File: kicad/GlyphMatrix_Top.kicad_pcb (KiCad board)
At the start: 2 copper layers, 294.9 x 128.6 mm, 74 parts

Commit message: added MCU
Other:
- board size 294.9 x 128.6 mm -> 295 x 128.6 mm

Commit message: screw holes
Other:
- board size 295 x 128.6 mm -> 294.9 x 128.6 mm

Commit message: pogo pin - ergogen
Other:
- board size 294.9 x 128.6 mm -> 295 x 128.6 mm

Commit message: changed screw sizes
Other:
- board size 295 x 128.6 mm -> 298.4 x 128.6 mm
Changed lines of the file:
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@@
   (title_block
     (title "GlyphMatrix_Top")
-    (date "2025-07-04")
-    (rev "0.3.6")
+    (date "2025-07-08")
+    (rev "0.4.3")
     (company "Allen Choi")
   )
@@
         (fp_rect (start -59.53125 -9.525) (end 59.53125 9.525) (stroke (width 0.1) (type solid)) (fill no) (layer "Dwgs.User") )
             )
-  (gr_line (start 60.875 202.3) (end 60.875 77.7125) (layer Edge.Cuts) (stroke (width 0.15) (type default)))
-(gr_line (start 62.875 75.7125) (end 353.82500000000005 75.7125) (layer Edge.Cuts) (stroke (width 0.15) (type default)))
-(gr_line (start 355.82500000000005 77.7125) (end 355.82500000000005 202.3) (layer Edge.Cuts) (stroke (width 0.15) (type default)))
-(gr_line (start 353.82500000000005 204.3) (end 62.875 204.3) (layer Edge.Cuts) (stroke (width 0.15) (type default)))
-(gr_arc (start 62.875 75.7125) (mid 61.4607864 76.29828640000001) (end 60.875 77.7125) (layer Edge.Cuts) (stroke (width 0.15) (type default)))
-(gr_arc (start 355.82500000000005 77.7125) (mid 355.2392136 76.29828640000001) (end 353.82500000000005 75.7125) (layer Edge.Cuts) (stroke (width 0.15) (type default)))
-(gr_arc (start 353.82500000000005 204.3) (mid 355.2392136 203.71421360000002) (end 355.82500000000005 202.3) (layer Edge.Cuts) (stroke (width 0.15) (type default)))
-(gr_arc (start 60.875 202.3) (mid 61.4607864 203.71421360000002) (end 62.875 204.3) (layer Edge.Cuts) (stroke (width 0.15) (type default)))
-(gr_circle (center 64.875 79.7125) (end 66.725 79.7125) (layer Edge.Cuts) (stroke (width 0.15) (type default)) (fill none))
-(gr_circle (center 351.82500000000005 79.7125) (end 353.67500000000007 79.7125) (layer Edge.Cuts) (stroke (width 0.15) (type default)) (fill none))
-(gr_circle (center 351.82500000000005 200.3) (end 353.67500000000007 200.3) (layer Edge.Cuts) (stroke (width 0.15) (type default)) (fill none))
-(gr_circle (center 64.875 200.3) (end 66.725 200.3) (layer Edge.Cuts) (stroke (width 0.15) (type default)) (fill none))
-(gr_circle (center 207.75 79.7125) (end 209.6 79.7125) (layer Edge.Cuts) (stroke (width 0.15) (type default)) (fill none))
-(gr_circle (center 214.73125000000002 190.0125) (end 216.58125 190.0125) (layer Edge.Cuts) (stroke (width 0.15) (type default)) (fill none))
-(gr_circle (center 151.21249999999998 141.625) (end 153.06249999999997 141.625) (layer Edge.Cuts) (stroke (width 0.15) (type default)) (fill none))
-(gr_circle (center 265.51250000000005 141.625) (end 267.36250000000007 141.625) (layer Edge.Cuts) (stroke (width 0.15) (type default)) (fill none))
+  (gr_line (start 59.175 202.3) (end 59.175 77.7125) (layer Edge.Cuts) (stroke (width 0.15) (type default)))
+(gr_line (start 61.175 75.7125) (end 355.52500000000003 75.7125) (layer Edge.Cuts) (stroke (width 0.15) (type default)))
+(gr_line (start 357.52500000000003 77.7125) (end 357.52500000000003 202.3) (layer Edge.Cuts) (stroke (width 0.15) (type default)))
+(gr_line (start 355.52500000000003 204.3) (end 61.175 204.3) (layer Edge.Cuts) (stroke (width 0.15) (type default)))
+(gr_arc (start 61.175 75.7125) (mid 59.7607864 76.29828640000001) (end 59.175 77.7125) (layer Edge.Cuts) (stroke (width 0.15) (type default)))
+(gr_arc (start 357.52500000000003 77.7125) (mid 356.9392136 76.29828640000001) (end 355.52500000000003 75.7125) (layer Edge.Cuts) (stroke (width 0.15) (type default)))
+(gr_arc (start 355.52500000000003 204.3) (mid 356.9392136 203.71421360000002) (end 357.52500000000003 202.3) (layer Edge.Cuts) (stroke (width 0.15) (type default)))
+(gr_arc (start 59.175 202.3) (mid 59.7607864 203.71421360000002) (end 61.175 204.3) (layer Edge.Cuts) (stroke (width 0.15) (type default)))
+(gr_circle (center 64.875 79.7125) (end 66.125 79.7125) (layer Edge.Cuts) (stroke (width 0.15) (type default)) (fill none))
+(gr_circle (center 351.82500000000005 79.7125) (end 353.07500000000005 79.7125) (layer Edge.Cuts) (stroke (width 0.15) (type default)) (fill none))
+(gr_circle (center 351.82500000000005 200.3) (end 353.07500000000005 200.3) (layer Edge.Cuts) (stroke (width 0.15) (type default)) (fill none))
+(gr_circle (center 64.875 200.3) (end 66.125 200.3) (layer Edge.Cuts) (stroke (width 0.15) (type default)) (fill none))
+(gr_circle (center 207.75 79.7125) (end 209 79.7125) (layer Edge.Cuts) (stroke (width 0.15) (type default)) (fill none))
+(gr_circle (center 214.73125000000002 190.0125) (end 215.98125000000002 190.0125) (layer Edge.Cuts) (stroke (width 0.15) (type default)) (fill none))
+(gr_circle (center 151.21249999999998 141.625) (end 152.46249999999998 141.625) (layer Edge.Cuts) (stroke (width 0.15) (type default)) (fill none))
+(gr_circle (center 265.51250000000005 141.625) (end 266.76250000000005 141.625) (layer Edge.Cuts) (stroke (width 0.15) (type default)) (fill none))
 )

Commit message: fixed positions for screw holes
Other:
- board size 298.4 x 128.6 mm -> 298.3 x 128.6 mm

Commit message: more tweaks  (#3)
* small tweaks

* GlyphMatrix - 3mm screws

* PhaseShift - 3mm screws

* DeltaForm - 3mm screws

* updated README.md
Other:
- outline, holes or cut-outs redrawn

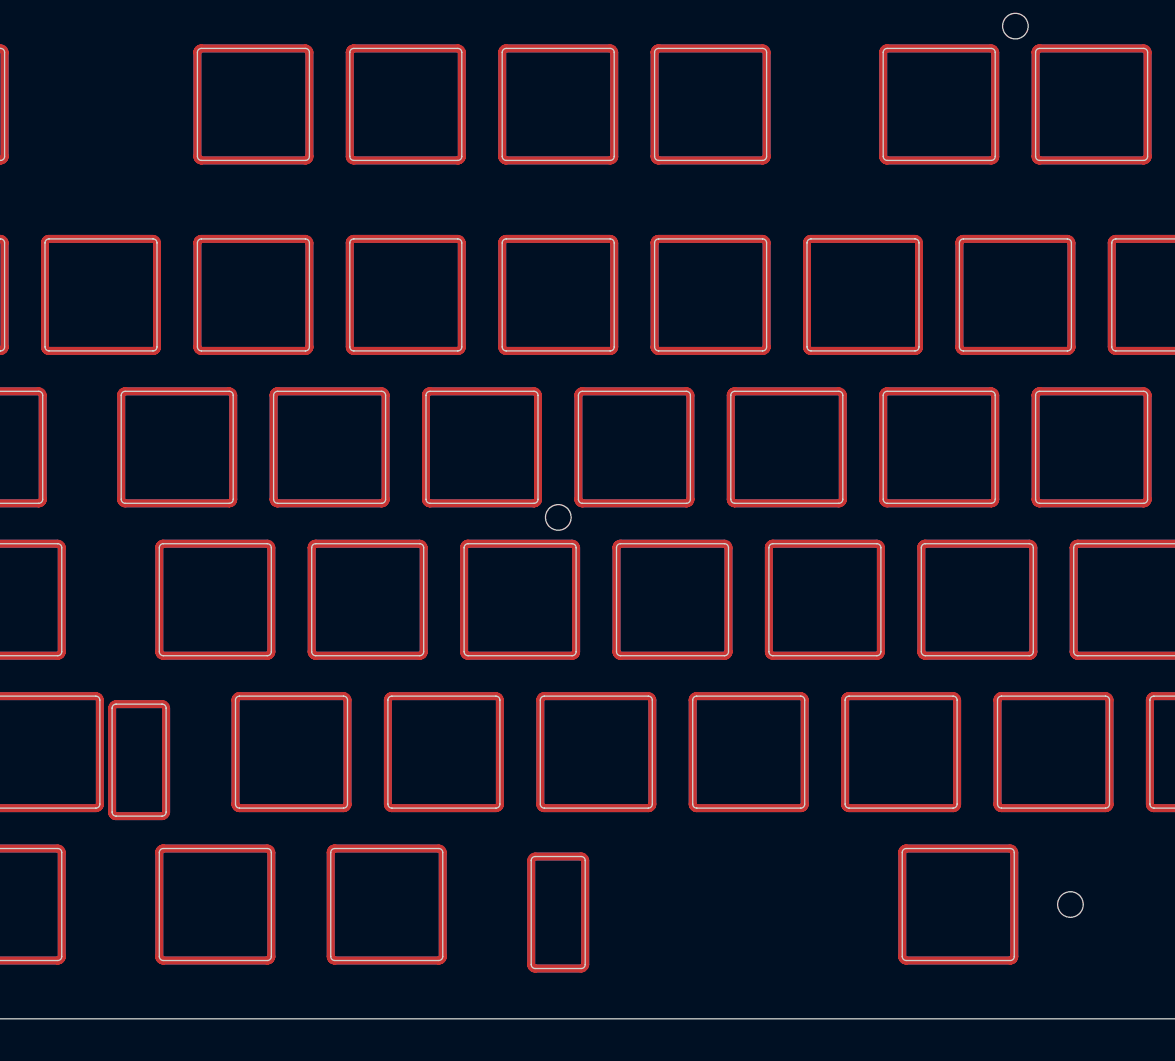
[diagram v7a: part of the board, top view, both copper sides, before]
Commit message: plates (#4)
* Silk Screen

* small changes for GlyphMatrix

* Silk screen for plates

* amended GlyphMatrix
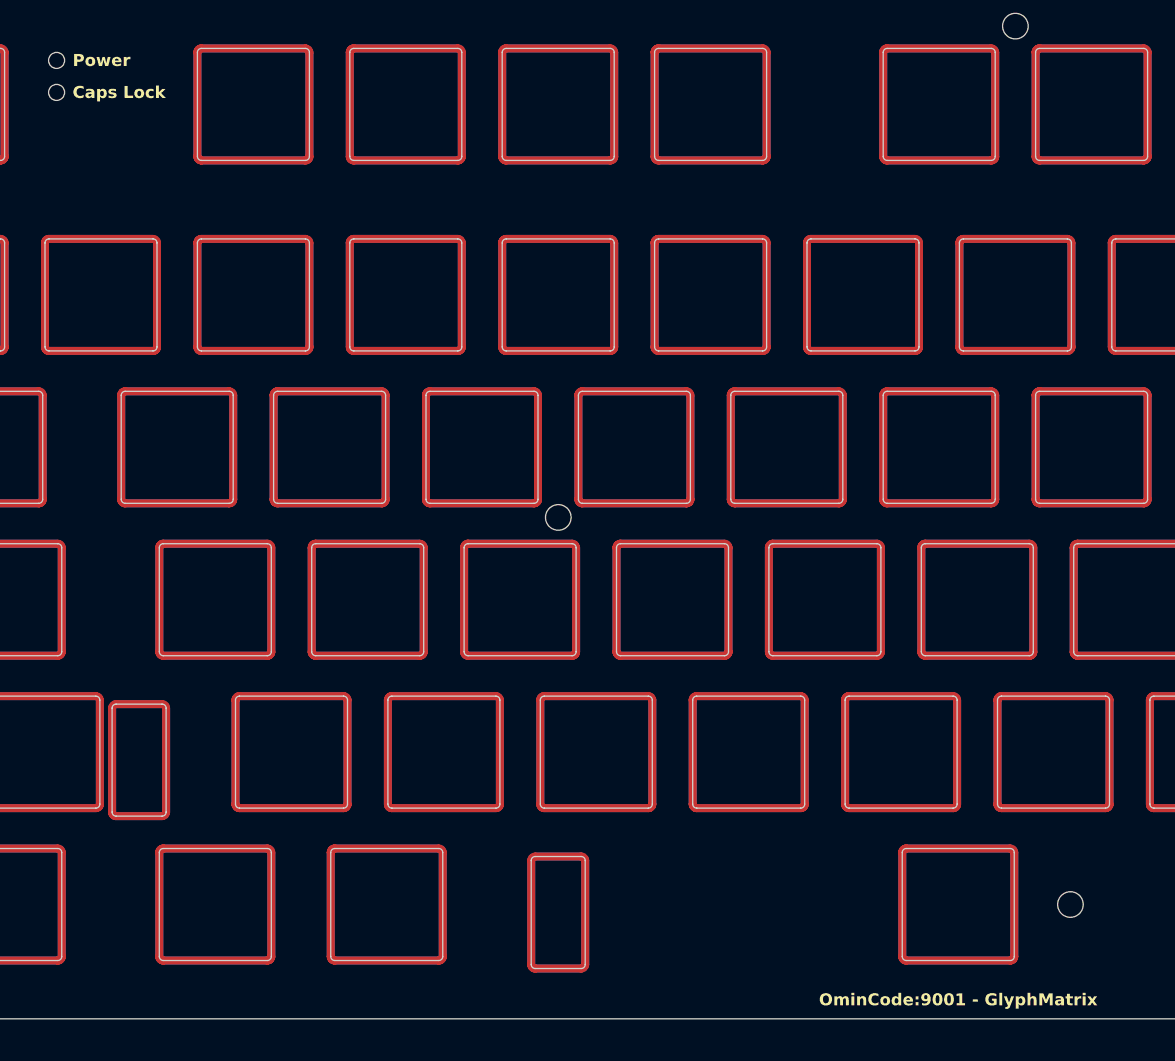
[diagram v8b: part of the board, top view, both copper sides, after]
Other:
- outline, holes or cut-outs redrawn
- board text added: "Caps Lock"
- board text added: "OminCode:9001 - GlyphMatrix"
- board text added: "Power"
